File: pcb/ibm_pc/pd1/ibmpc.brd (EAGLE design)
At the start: 56 x 65 mm, 47 parts, among them IC1 STM32F072C8T6, SW1 324_SW, SW2 324_SW, U1 MAX3232

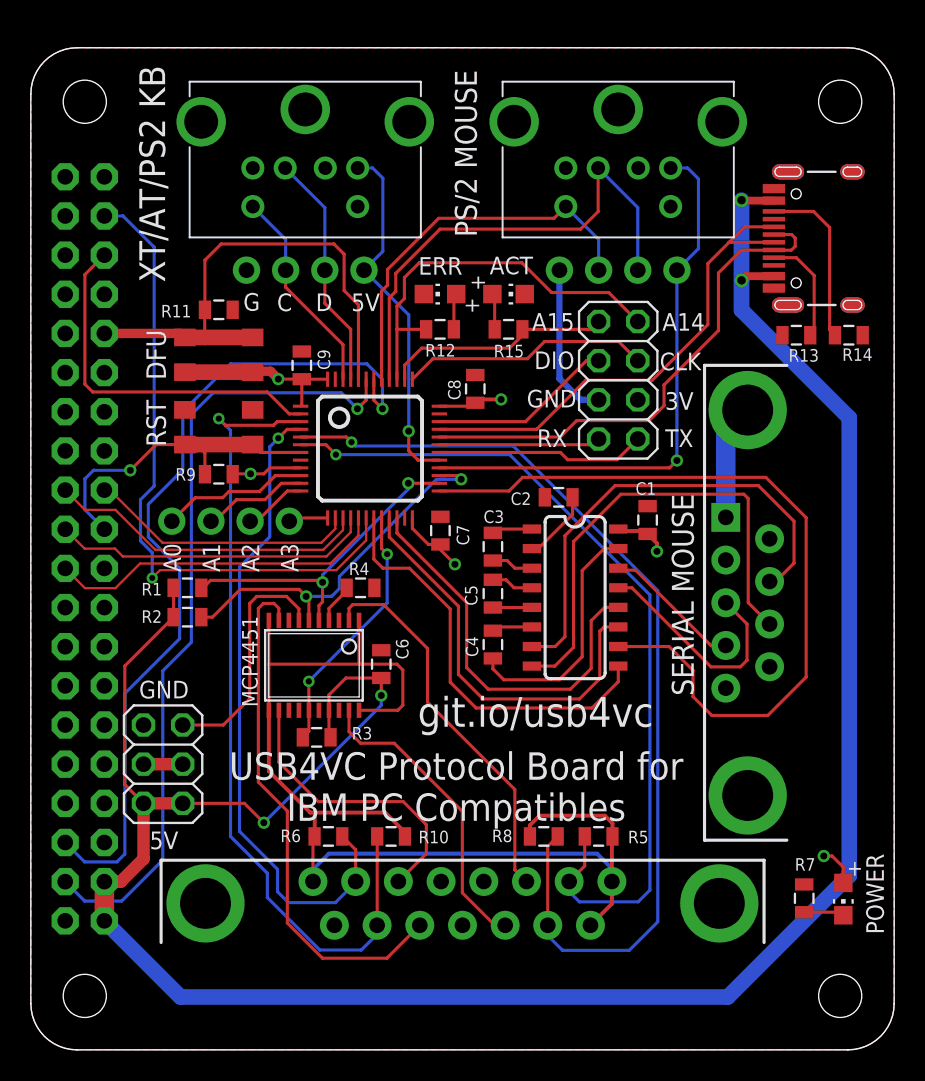
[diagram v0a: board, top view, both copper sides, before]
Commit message: added BUSY to ibm card
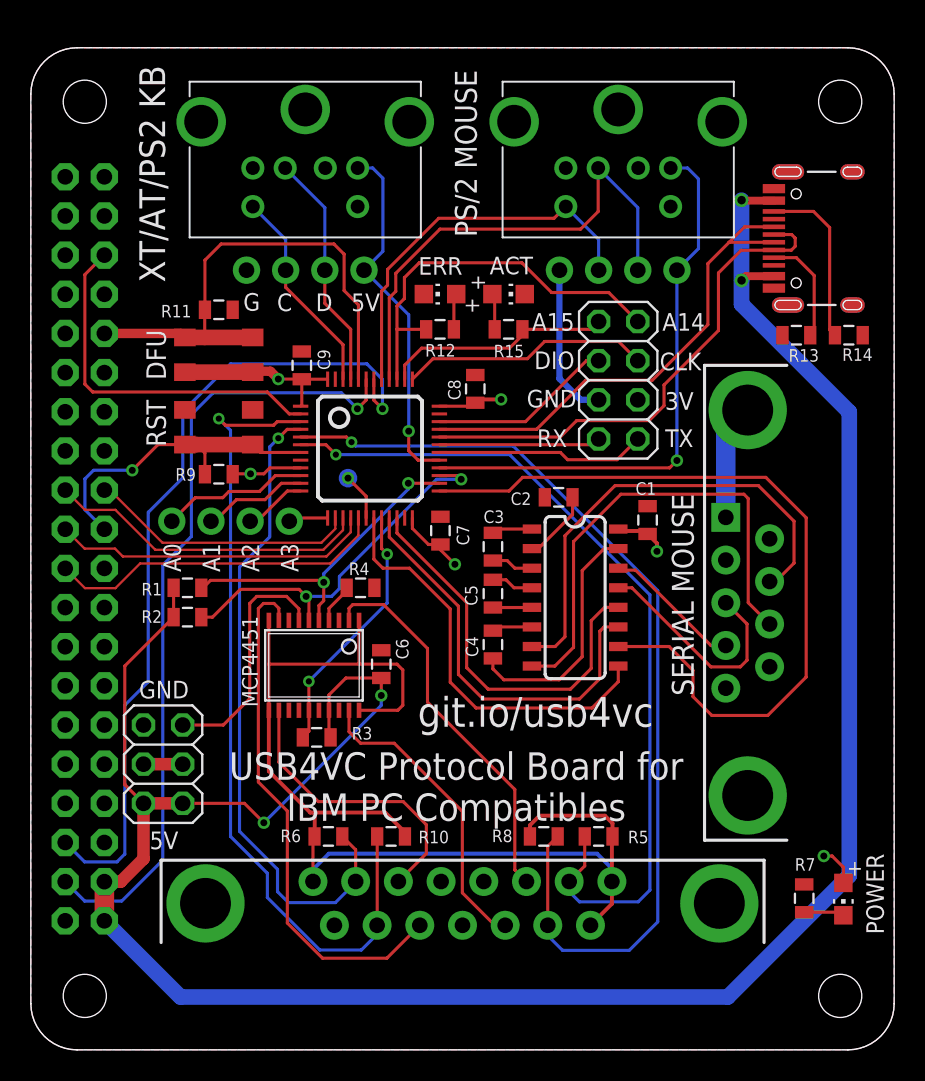
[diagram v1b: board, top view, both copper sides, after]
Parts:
- added TP3: TPTP12R, testpad:TP12R
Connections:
- removed net N$3: IC1.18, JP1.38
- new net N$45: IC1.18, TP3.TP
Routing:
- net N$3: track 42.6 -> 0.00 mm, vias 1 -> 0
- net N$45: track 0.00 -> 3.07 mm, vias 0 -> 1
- net N$22: track 55.3 -> 53.6 mm
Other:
- board text added: "B0"
- board text added: "git.io/usb4vc dekuNukem PD1 MAR 2022"
- board text removed: "git.io/usb4vc dekuNukem PD2 MAR 2023"
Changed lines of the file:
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@@
 <text x="14.2494" y="31.9278" size="1.143" layer="25" rot="R270" align="center">A2</text>
 <text x="16.7894" y="31.9278" size="1.143" layer="25" rot="R270" align="center">A3</text>
+<text x="20.5994" y="35.2806" size="1.143" layer="26" rot="MR270" align="center">B0</text>
 <text x="28" y="3.81" size="1.6764" layer="26" rot="MR180" align="center">git.io/usb4vc
-dekuNukem PD2 MAR 2023</text>
+dekuNukem PD1 MAR 2022</text>
 <text x="32.7406" y="21.9202" size="1.9304" layer="25" rot="R180" align="center">git.io/usb4vc</text>
 <text x="8.636" y="23.368" size="1.143" layer="25" rot="R180" align="center">GND</text>
@@
 </element>
 <element name="U$10" library="adafruit_changed" package="1X04-CLEANBIG" value="PINHD1X4" x="12.954" y="34.29" smashed="yes"/>
+<element name="TP3" library="testpad" library_urn="urn:adsk.eagle:library:385" package="TP12R" package3d_urn="urn:adsk.eagle:package:27963/1" value="TPTP12R" x="20.574" y="37.084" smashed="yes" rot="MR0">
+<attribute name="POPULARITY" value="1" x="20.574" y="37.084" size="1.778" layer="28" rot="MR0" display="off"/>
+<attribute name="TP_SIGNAL_NAME" value="" x="20.574" y="37.084" size="1.778" layer="28" rot="MR0" display="off"/>
+</element>
 <element name="R1" library="SparkFun-Passives" package="0805" value="5.1K" x="10.16" y="29.972" smashed="yes">
 <attribute name="NAME" x="8.509" y="30.2895" size="0.8128" layer="25" rot="R180"/>
@@
 <wire x1="10.7442" y1="39.261" x2="11.292" y2="38.7132" width="0.2032" layer="1"/>
 <wire x1="11.292" y1="38.7132" x2="11.292" y2="37.338" width="0.2032" layer="1"/>
-<via x="6.4516" y="37.592" extent="1-16" drill="0.45"/>
-<wire x1="6.4516" y1="37.592" x2="8.1206" y2="39.261" width="0.2032" layer="1"/>
-<wire x1="8.1206" y1="39.261" x2="9.992" y2="39.261" width="0.2032" layer="1"/>
+<via x="6.5786" y="37.592" extent="1-16" drill="0.45"/>
+<wire x1="6.5786" y1="37.592" x2="8.2476" y2="39.261" width="0.2032" layer="1"/>
+<wire x1="8.2476" y1="39.261" x2="9.992" y2="39.261" width="0.2032" layer="1"/>
 <wire x1="4.064" y1="37.592" x2="3.5052" y2="37.0332" width="0.2032" layer="16"/>
 <wire x1="3.5052" y1="37.0332" x2="3.5052" y2="35.0348" width="0.2032" layer="16"/>
 <wire x1="3.5052" y1="35.0348" x2="4.77" y2="33.77" width="0.2032" layer="16"/>
-<wire x1="6.4516" y1="37.592" x2="4.064" y2="37.592" width="0.2032" layer="16"/>
+<wire x1="6.5786" y1="37.592" x2="4.064" y2="37.592" width="0.2032" layer="16"/>
 </signal>
 <signal name="+5V">
@@
 <wire x1="53.086" y1="11.303" x2="45.212" y2="3.429" width="1.016" layer="16"/>
 <via x="46.101" y="49.911" extent="1-16" drill="0.55"/>
-<wire x1="53.086" y1="40.9956" x2="53.086" y2="11.303" width="1.016" layer="16"/>
-<wire x1="46.101" y1="47.9806" x2="53.086" y2="40.9956" width="1.016" layer="16"/>
-<wire x1="46.101" y1="47.9806" x2="46.101" y2="49.911" width="1.016" layer="16"/>
+<wire x1="53.086" y1="41.3766" x2="53.086" y2="11.303" width="1.016" layer="16"/>
+<wire x1="46.101" y1="48.3616" x2="53.086" y2="41.3766" width="1.016" layer="16"/>
+<wire x1="46.101" y1="48.3616" x2="46.101" y2="49.911" width="1.016" layer="16"/>
 <wire x1="46.101" y1="55.118" x2="46.101" y2="49.911" width="1.016" layer="16"/>
 <wire x1="48.2" y1="50.185" x2="46.375" y2="50.185" width="0.508" layer="1"/>
@@
 <wire x1="21.7932" y1="44.5008" x2="12.954" y2="44.5008" width="0.2032" layer="16"/>
 <wire x1="12.954" y1="44.5008" x2="9.8552" y2="41.402" width="0.2032" layer="16"/>
-<wire x1="9.8552" y1="37.6174" x2="7.62" y2="35.3822" width="0.2032" layer="16"/>
-<wire x1="9.8552" y1="41.402" x2="9.8552" y2="37.6174" width="0.2032" layer="16"/>
+<wire x1="9.8552" y1="37.1094" x2="7.62" y2="34.8742" width="0.2032" layer="16"/>
+<wire x1="9.8552" y1="41.402" x2="9.8552" y2="37.1094" width="0.2032" layer="16"/>
+<wire x1="7.62" y1="34.8742" x2="7.62" y2="23.876" width="0.2032" layer="16"/>
+<wire x1="6.096" y1="22.352" x2="6.096" y2="12.7" width="0.2032" layer="16"/>
 <wire x1="6.096" y1="12.7" x2="5.588" y2="12.192" width="0.2032" layer="16"/>
 <wire x1="5.588" y1="12.192" x2="3.488" y2="12.192" width="0.2032" layer="16"/>
-<wire x1="7.62" y1="35.3822" x2="7.62" y2="33.274" width="0.2032" layer="16"/>
-<wire x1="7.62" y1="33.274" x2="9.652" y2="31.242" width="0.2032" layer="16"/>
-<wire x1="9.652" y1="31.242" x2="9.652" y2="26.67" width="0.2032" layer="16"/>
-<wire x1="9.652" y1="26.67" x2="6.096" y2="23.114" width="0.2032" layer="16"/>
-<wire x1="6.096" y1="23.114" x2="6.096" y2="12.7" width="0.2032" layer="16"/>
+<wire x1="7.62" y1="23.876" x2="6.096" y2="22.352" width="0.2032" layer="16"/>
 </signal>
 <signal name="N$23">
@@
 <wire x1="3.488" y1="9.652" x2="2.23" y2="10.91" width="0.2032" layer="16"/>
 <wire x1="5.8928" y1="9.652" x2="3.488" y2="9.652" width="0.2032" layer="16"/>
-<wire x1="10.414" y1="41.1988" x2="10.414" y2="26.4414" width="0.2032" layer="16"/>
-<wire x1="10.414" y1="26.4414" x2="8.5598" y2="24.5872" width="0.2032" layer="16"/>
-<wire x1="8.5598" y1="24.5872" x2="8.5598" y2="12.319" width="0.2032" layer="16"/>
+<wire x1="10.414" y1="41.1988" x2="10.414" y2="33.2994" width="0.2032" layer="16"/>
+<wire x1="10.414" y1="33.2994" x2="8.5598" y2="31.4452" width="0.2032" layer="16"/>
+<wire x1="8.5598" y1="31.4452" x2="8.5598" y2="12.319" width="0.2032" layer="16"/>
 <wire x1="8.5598" y1="12.319" x2="5.8928" y2="9.652" width="0.2032" layer="16"/>
 </signal>
@@
 <via x="24.4856" y="36.7538" extent="1-16" drill="0.45"/>
 <wire x1="24.4856" y1="36.7538" x2="24.4856" y2="36.3728" width="0.2032" layer="16"/>
-<wire x1="24.4856" y1="36.3728" x2="18.923" y2="30.8102" width="0.2032" layer="16"/>
-<wire x1="18.923" y1="30.8102" x2="18.923" y2="30.3276" width="0.2032" layer="16"/>
-<via x="18.923" y="30.3276" extent="1-16" drill="0.45"/>
-<wire x1="18.923" y1="30.3276" x2="18.923" y2="29.0576" width="0.2032" layer="1"/>
+<wire x1="24.4856" y1="36.3728" x2="18.9992" y2="30.8864" width="0.2032" layer="16"/>
+<wire x1="18.9992" y1="30.8864" x2="18.9992" y2="30.3276" width="0.2032" layer="16"/>
+<via x="18.9992" y="30.3276" extent="1-16" drill="0.45"/>
+<wire x1="18.9992" y1="30.3276" x2="18.9992" y2="29.1338" width="0.2032" layer="1"/>
 <wire x1="18.6892" y1="28.8238" x2="18.6892" y2="27.8606" width="0.2032" layer="1"/>
-<wire x1="18.923" y1="29.0576" x2="18.6892" y2="28.8238" width="0.2032" layer="1"/>
+<wire x1="18.9992" y1="29.1338" x2="18.6892" y2="28.8238" width="0.2032" layer="1"/>
 <contactref element="R1" pad="2"/>
-<wire x1="18.923" y1="30.3276" x2="18.796" y2="30.4546" width="0.2032" layer="1"/>
+<wire x1="18.9992" y1="30.3276" x2="18.8722" y2="30.4546" width="0.2032" layer="1"/>
 <wire x1="11.118" y1="29.914" x2="11.06" y2="29.972" width="0.2032" layer="1"/>
-<wire x1="18.796" y1="30.4546" x2="11.6586" y2="30.4546" width="0.2032" layer="1"/>
+<wire x1="18.8722" y1="30.4546" x2="11.6586" y2="30.4546" width="0.2032" layer="1"/>
 <wire x1="11.6586" y1="30.4546" x2="11.118" y2="29.914" width="0.2032" layer="1"/>
 </signal>
@@
 <wire x1="18.0392" y1="22.025" x2="18.0392" y2="20.6664" width="0.2032" layer="1"/>
 <wire x1="18.0392" y1="20.6664" x2="17.642" y2="20.2692" width="0.2032" layer="1"/>
+</signal>
+<signal name="N$45">
+<contactref element="TP3" pad="TP"/>
+<contactref element="IC1" pad="18"/>
+<wire x1="21.75" y1="34.5" x2="21.75" y2="35.908" width="0.2032" layer="1"/>
+<wire x1="21.75" y1="35.908" x2="20.574" y2="37.084" width="0.2032" layer="1"/>
+<via x="20.574" y="37.084" extent="1-16" drill="0.45"/>
 </signal>
 <signal name="N$31">
@@
 <wire x1="31.3944" y1="16.891" x2="31.3944" y2="11.6756" width="0.2032" layer="1"/>
 </signal>
-<signal name="N$3">
-<contactref element="IC1" pad="18"/>
-<contactref element="JP1" pad="38"/>
-<wire x1="21.75" y1="34.5" x2="21.75" y2="33.053" width="0.1524" layer="1"/>
-<via x="7.874" y="30.607" extent="1-16" drill="0.381"/>
-<wire x1="21.75" y1="33.053" x2="19.812" y2="31.115" width="0.1524" layer="1"/>
-<wire x1="19.812" y1="31.115" x2="8.382" y2="31.115" width="0.1524" layer="1"/>
-<wire x1="8.382" y1="31.115" x2="7.874" y2="30.607" width="0.1524" layer="1"/>
-<wire x1="7.874" y1="30.607" x2="7.874" y2="32.258" width="0.2032" layer="16"/>
-<wire x1="7.874" y1="32.258" x2="7.112" y2="33.02" width="0.2032" layer="16"/>
-<wire x1="7.112" y1="35.687" x2="8.001" y2="36.576" width="0.2032" layer="16"/>
-<wire x1="8.001" y1="36.576" x2="8.001" y2="52.07" width="0.2032" layer="16"/>
-<wire x1="5.981" y1="54.09" x2="4.77" y2="54.09" width="0.2032" layer="16"/>
-<wire x1="7.112" y1="33.02" x2="7.112" y2="35.687" width="0.2032" layer="16"/>
-<wire x1="8.001" y1="52.07" x2="5.981" y2="54.09" width="0.2032" layer="16"/>
-</signal>
 </signals>
